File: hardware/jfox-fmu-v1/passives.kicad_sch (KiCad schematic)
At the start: 74 parts, among them X1 16MHz, X2 32.768kHz

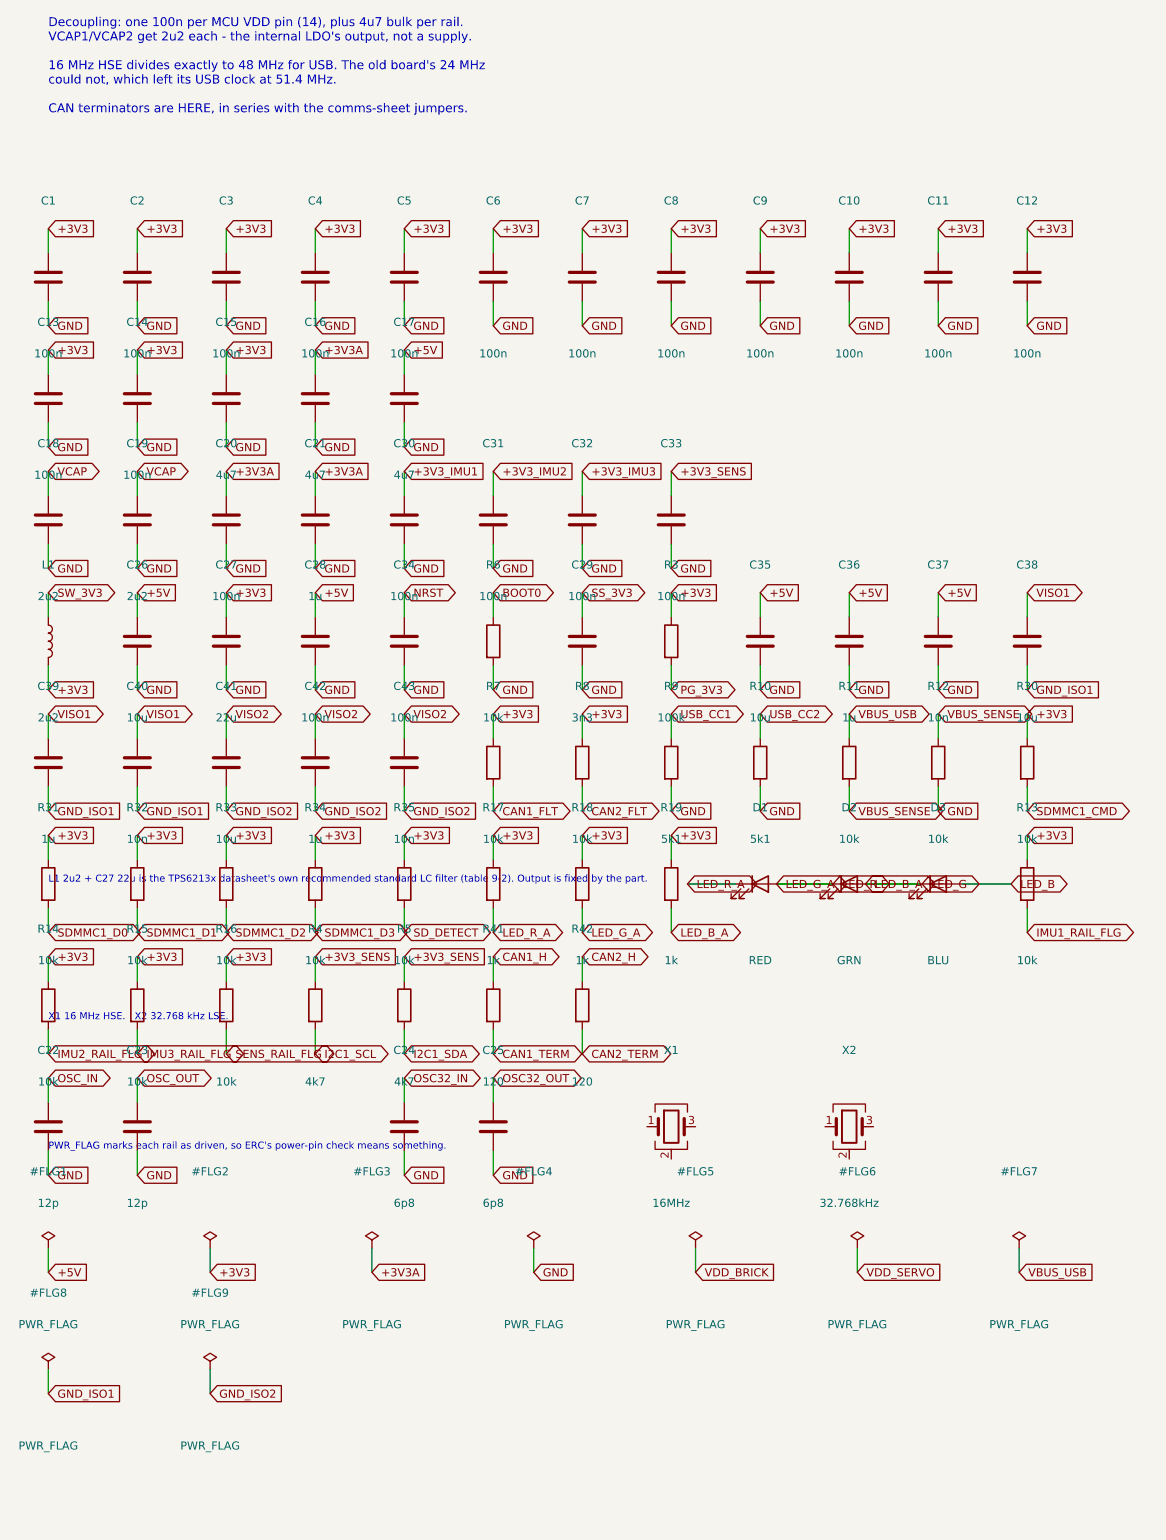
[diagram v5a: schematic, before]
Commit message: Card-cage TMR: FCU becomes a plug-in card, backplane carries the I/O
The FMU stops being a module that mates face-to-face with a base board
underneath it and becomes a card that slides into a backplane. That change
came from the JFOX FCU V1 sketch, and it dissolved a constraint I had
worked around rather than removed: the DF12 mezzanine's 3.0 mm stack height
joins two adjacent boards only, so three channels each needing an
independent path to one base board could not use it. Riser cards were the
workaround. Mating at the card's rear edge means nothing has to span the
gap, so the risers and their extra mated pair per channel are gone.

FCU card, 40 x 90 mm (was 100 x 80):
  * 58-contact Samtec MECF-30 card edge, polarised. Contacts 21/22 are a
    1.24 x 7.0 mm key notch offset from centre - a card the wrong way round
    physically will not enter, which is the only insertion safeguard that
    works before power is applied. Two grounds were sacrificed for it out of
    twenty rather than any signal.
  * Power input tree (LTC4417, six ORing FETs, dividers, input TVS) and the
    debug header move to the backplane. The card receives an already-ORed,
    already-fused +5V_CARRIER on three fingers.
  * Front edge carries everything a person touches: microSD, USB-C, and two
    lamps flanking it. D1 is hardwired to the rail so it lights with no
    firmware running - a power lamp the MCU drives tells you the MCU is
    alive, which is not what anyone reads it for.
  * Power and isolated blocks moved to the back face. Both noise groups are
    grouped at one end so the sensor island can sit 22 mm clear at the
    other; spread out, every point on an 80 mm body is within 13 mm of
    something switching.

JFOX-BASE-v1 backplane, 100 x 100 mm, new:
  * Three independent card-edge sockets in a column. A bent contact in one
    slot costs one channel; a shared bus would cost all three and leave the
    voter nothing to vote on.
  * Two airframe feeds at opposite corners, ORed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
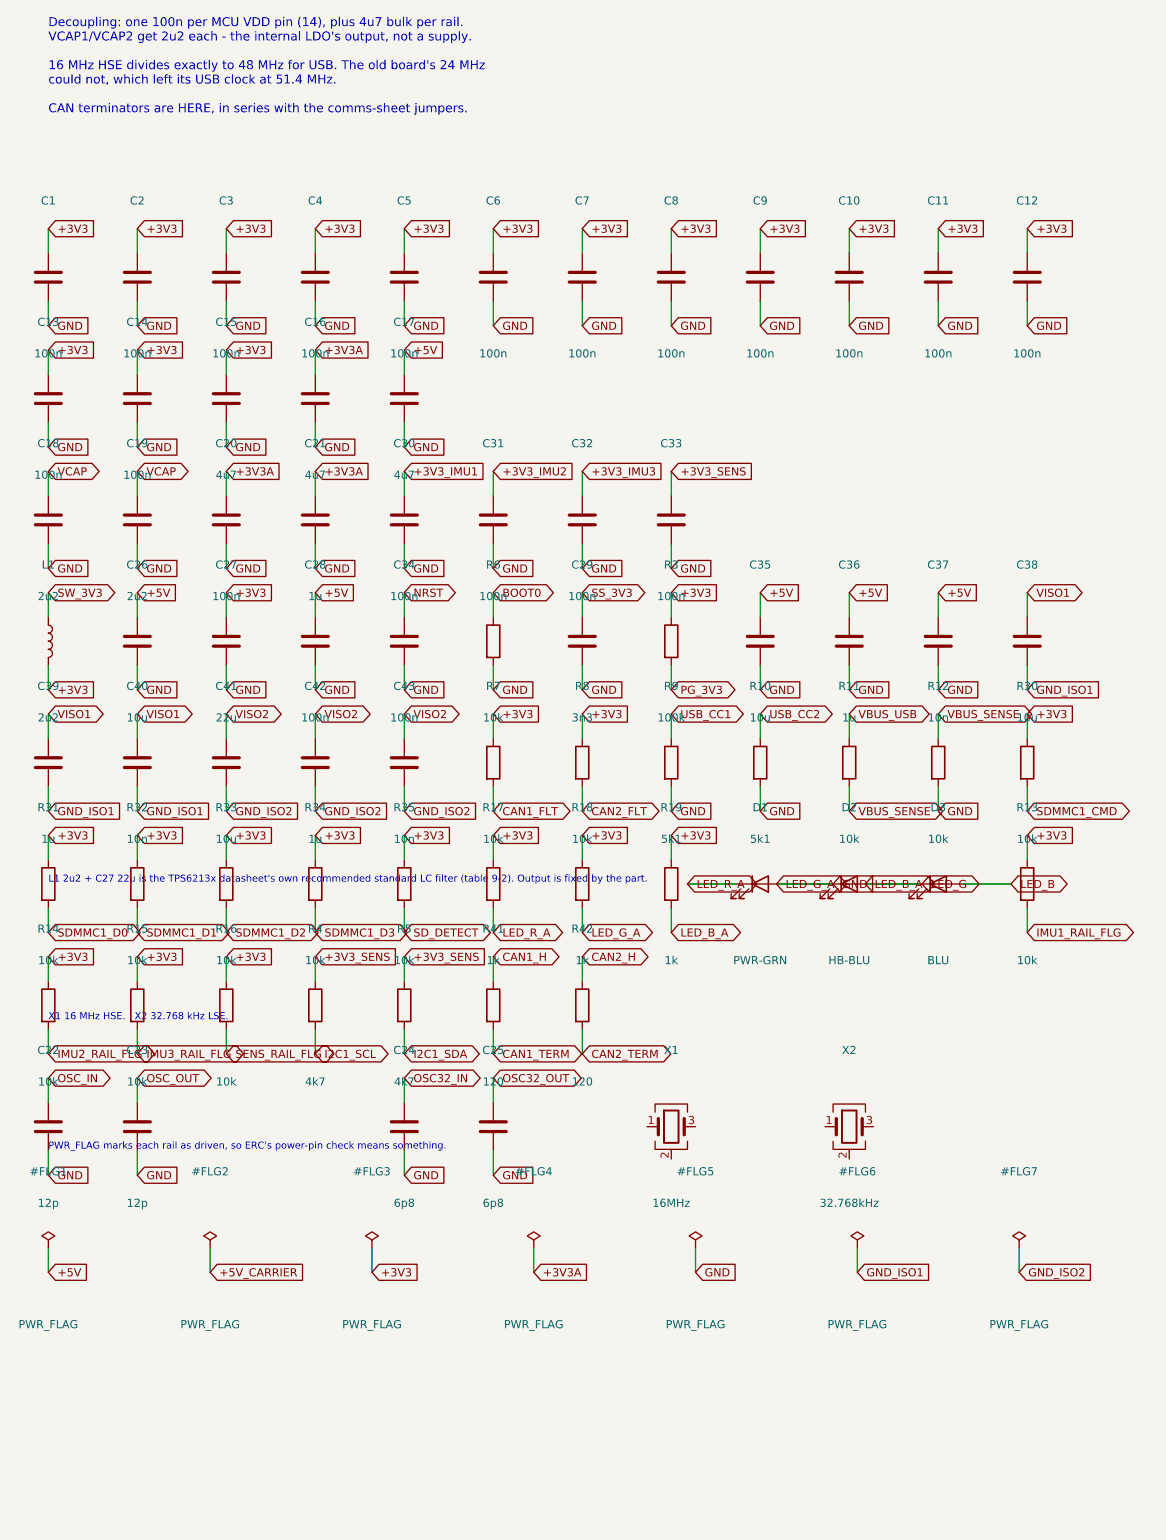
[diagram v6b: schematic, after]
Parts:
- D1: value RED -> PWR-GRN; footprint LED_SMD:LED_0603_1608Metric -> LED_SMD:LED_0402_1005Metric
- D2: value GRN -> HB-BLU; footprint LED_SMD:LED_0603_1608Metric -> LED_SMD:LED_0402_1005Metric
- D3: footprint LED_SMD:LED_0603_1608Metric -> LED_SMD:LED_0402_1005Metric
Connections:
- net LED_G_A is gone; now on net GND: D1.2 (A), D2.1 (K), R18.2
